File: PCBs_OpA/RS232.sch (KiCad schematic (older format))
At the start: 9 parts, among them J3 USB_B, U3 FT232RL

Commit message: ADX988 CAT: add FE, FI commands
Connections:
- net at J3.2 (D-): now also U3.16 (USBD-); no longer U3.15 (USBD+)
- net at J3.3 (D+): now also U3.15 (USBD+); no longer U3.16 (USBD-)
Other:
- moved on the sheet: J3
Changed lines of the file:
@@
 L USB_B J3
 U 1 1 630B7FAF
-P 8500 2350
-F 0 "J3" H 8300 2800 50  0000 L CNN
-F 1 "USB_B" H 8300 2700 50  0000 L CNN
-F 2 "Connectors:USB_B" H 8650 2300 50  0001 C CNN
-F 3 "" H 8650 2300 50  0001 C CNN
-	1    8500 2350
+P 8000 2450
+F 0 "J3" H 7800 2900 50  0000 L CNN
+F 1 "USB_B" H 7800 2800 50  0000 L CNN
+F 2 "Connectors:USB_B" H 8150 2400 50  0001 C CNN
+F 3 "" H 8150 2400 50  0001 C CNN
+	1    8000 2450
 	-1   0    0    -1
 $EndComp
@@
 L GND #PWR0113
 U 1 1 630B8385
-P 8550 2850
-F 0 "#PWR0113" H 8550 2600 50  0001 C CNN
-F 1 "GND" H 8550 2700 50  0001 C CNN
-F 2 "" H 8550 2850 50  0001 C CNN
-F 3 "" H 8550 2850 50  0001 C CNN
-	1    8550 2850
+P 8050 2950
+F 0 "#PWR0113" H 8050 2700 50  0001 C CNN
+F 1 "GND" H 8050 2800 50  0001 C CNN
+F 2 "" H 8050 2950 50  0001 C CNN
+F 3 "" H 8050 2950 50  0001 C CNN
+	1    8050 2950
 	1    0    0    -1
 $EndComp
 Wire Wire Line
-	8500 2750 8500 2800
+	8000 2850 8000 2900
 Wire Wire Line
-	8500 2800 8600 2800
+	8000 2900 8100 2900
 Wire Wire Line
-	8600 2800 8600 2750
+	8100 2900 8100 2850
 Wire Wire Line
-	8550 2800 8550 2850
-Connection ~ 8550 2800
-Wire Wire Line
-	6550 2350 8200 2350
-Wire Wire Line
-	6300 2450 8200 2450
+	8050 2900 8050 2950
+Connection ~ 8050 2900
 $Comp
 L FT232RL U3
@@
 Wire Wire Line
 	5700 2750 6550 2750
-Wire Wire Line
-	6550 2750 6550 2350
 Wire Wire Line
 	5900 1900 5900 3150
@@
 Wire Wire Line
 	3850 2000 3850 2350
+Wire Wire Line
+	6300 2450 7700 2450
+Wire Wire Line
+	7700 2550 6550 2550
+Wire Wire Line
+	6550 2550 6550 2750
 $EndSCHEMATC

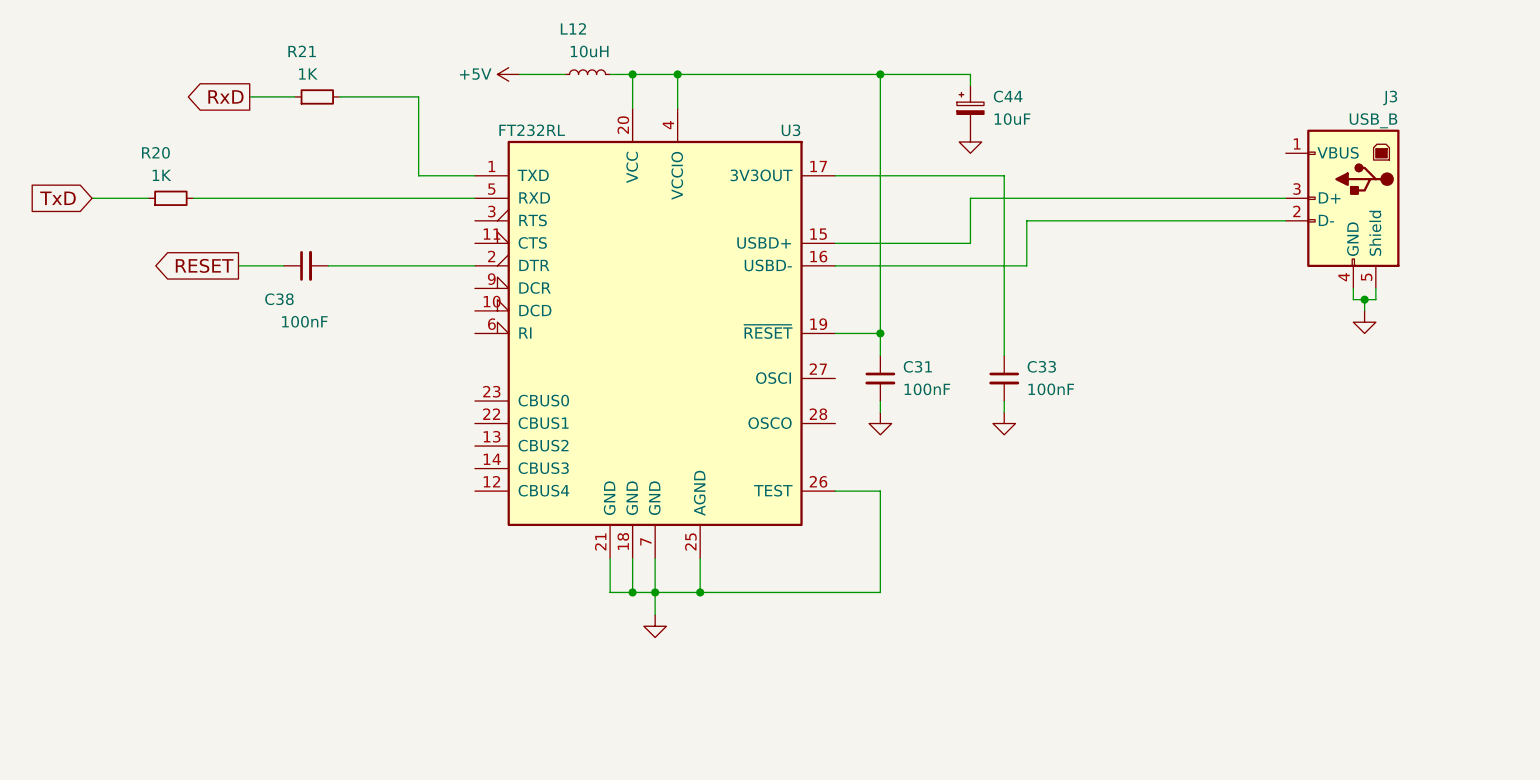
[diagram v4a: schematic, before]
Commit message: Arduino Nano PCB ADX988 DSP
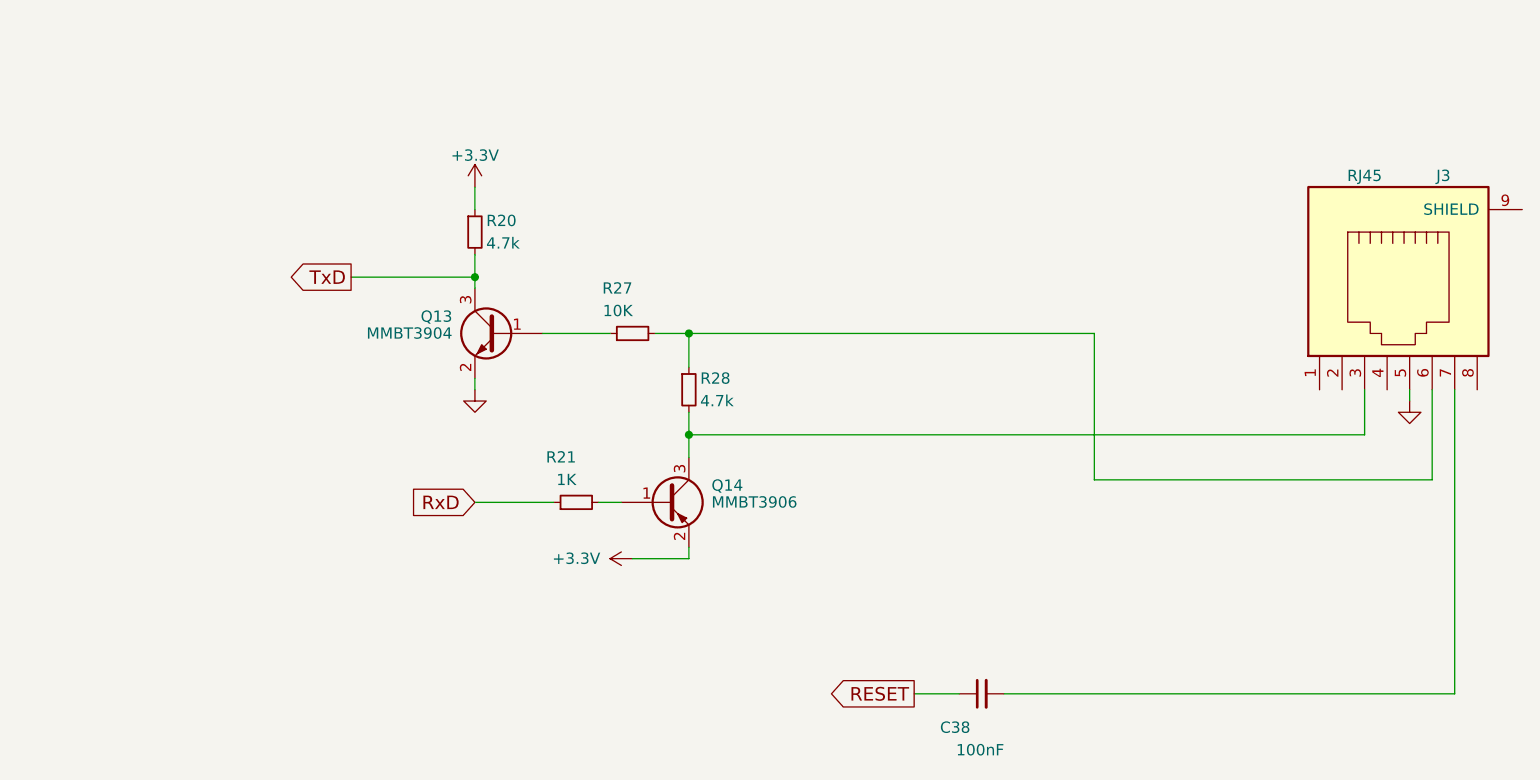
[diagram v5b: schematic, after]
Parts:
- removed C31, C33: 100nF, LCSDR:C_1206_0603, symbol C_Small
- removed C44: 10uF, Capacitors_THT:CP_Radial_D5.0mm_P2.00mm, symbol CP_Small
- removed J3: USB_B, Connectors:USB_B, symbol USB_B
- removed L12: 10uH, Choke_Axial_ThroughHole:Choke_Horizontal_RM10mm, symbol L_Small
- removed U3: FT232RL, Housings_SSOP:SSOP-28_5.3x10.2mm_Pitch0.65mm, symbol FT232RL
- added J3: RJ45, Connectors:RJ45_8, symbol RJ45
- added Q13: MMBT3904, TO_SOT_Packages_SMD:SOT-23, symbol MMBT3904
- added Q14: MMBT3906, TO_SOT_Packages_SMD:SOT-23, symbol MMBT3906
- added R27: 10K, Resistors_SMD:R_0603_HandSoldering, symbol R_Small
- added R28: 4.7k, Resistors_SMD:R_0603_HandSoldering, symbol R_Small
- R20: value 1K -> 4.7k
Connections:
- net GND: now also J3.5, Q13.2 (E)
- net TxD: now also R20.2, Q13.3 (C); no longer R20.1
- net at C38.2: now also J3.7
- net at R21.2: now also Q14.1 (B)
- new net: J3.3, Q14.3 (C), R28.2
- new net: J3.6, R27.2, R28.1
- new net: Q13.1 (B), R27.1
- new net +3V3: Q14.2 (E), R20.1
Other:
- moved on the sheet: C38
